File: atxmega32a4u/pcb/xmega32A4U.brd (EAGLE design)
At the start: 51.8 x 18.8 mm, 15 parts

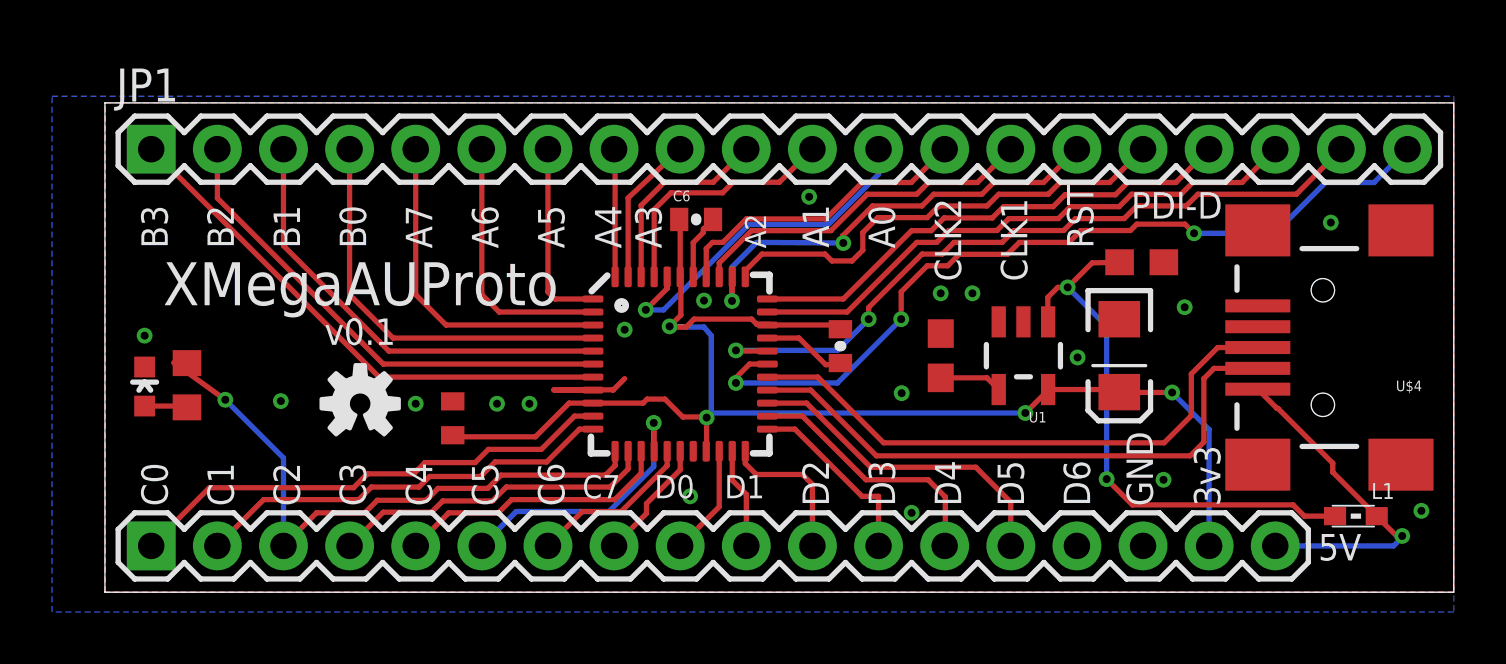
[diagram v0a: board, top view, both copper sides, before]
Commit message: Fix ciruit errors in LDO, added ESD protection to USB circuit - this will be v0.3
v0.3 ready
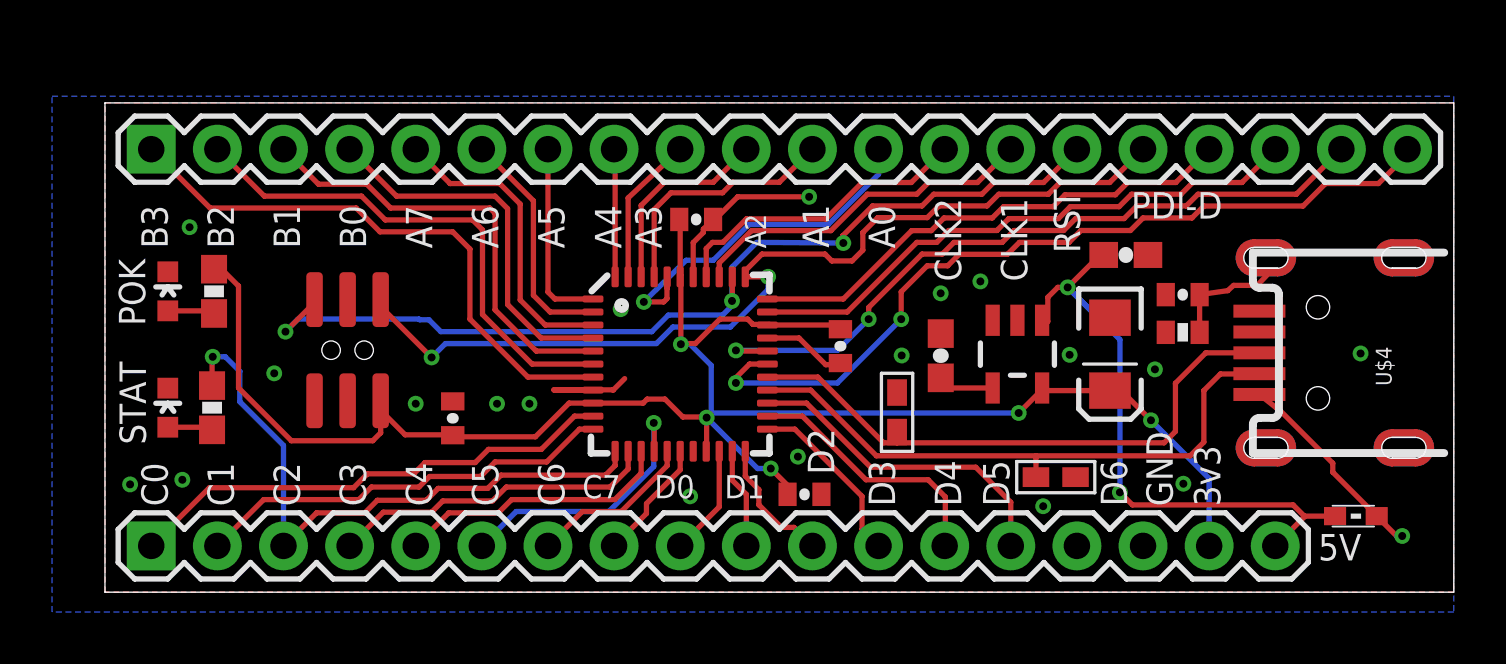
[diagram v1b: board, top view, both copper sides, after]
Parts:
- removed LED2: Blue, SparkFun-LED:LED-0603
- added C4, C7: 0.1uF, SparkFun-Capacitors:0402-CAP
- added ESD1, ESD2: CG0603MLC-05E, JCM:0603-CHIPGUARD
- added POK: Green, SparkFun-LED:LED-0603
- added R2: 1M, SparkFun-Resistors:0402-RES
- added R3: 1k, SparkFun-Passives:0603-RES
- added STATUS: Blue, SparkFun-LED:LED-0603
- added U$7: AVR_PDI_PROG, JCM:AVR_50MIL_PROG
- C1, C3: device rcl:C0603 -> SparkFun-Capacitors:0603-CAP
- C2: device SparkFun-Passives:EIA3216 -> SparkFun-Capacitors:EIA3216
- C5, C6: value (none) -> 0.1uF; device SparkFun-Passives:0402-CAP -> SparkFun-Capacitors:0402-CAP
- C8: value 0.1uF -> 4.7nF; device rcl:C0402 -> SparkFun-Capacitors:0402-CAP
- R1: value 330 -> 1k; device adafruit:R0603 -> SparkFun-Passives:0603-RES
- U$4: value USB-MINIB-5PIN -> USB-MINIB; device SparkFun-Connectors:USB-MINIB -> JCM-Connectors:USB-MINI-B-UX60-MB-5S8
- moved C8 28.4 mm to (42.2, 12.2), turned to 0 degrees
- moved U$6 6.95 mm to (16.4, 11.8), flipped to the bottom
- moved U$4 2.45 mm to (45.1, 9.96), turned to 90 degrees
- moved R1 1.30 mm to (4.88, 7.85)
- moved C1 0.67 mm to (40.0, 13.7)
- moved C2 0.36 mm to (39.4, 9.91)
- moved U1 0.24 mm to (35.8, 9.91)
- renumbered U$1 to UC, U$5 to JP2
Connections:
- new net N$1: POK.A, R3.2
- new net SHLD: C8.2, R2.2, U$4.SHLD1, U$4.SHLD2, U$4.SHLD3, U$4.SHLD4
- net 3.3V: now also C4.1, C7.1, R3.1, U$7.2; no longer C8.1
- net 5V: no longer JP2.18
- net 5VINT: now also JP2.18, U1.3
- net GND: now also C4.2, C7.2, C8.1, ESD1.P$1, ESD2.P$1, POK.C, R2.1, STATUS.C, U$7.6; no longer C8.2, LED2.C
- net N$2: now also STATUS.A; no longer LED2.A
- net PD6/D-: now also ESD1.P$2
- net PD7/D+: now also ESD2.P$2
- net PDI-DATA: now also U$7.1
- net RST: now also U$7.5
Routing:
- net RST: track 17.6 -> 37.4 mm, vias 2 -> 3
- net PDI-DATA: track 17.8 -> 36.2 mm, vias 0 -> 2
- net 3.3V: track 53.7 -> 72.0 mm, vias 4 -> 5
- net 5V: track 13.1 -> 7.96 mm
- net SHLD: track 0.00 -> 4.45 mm
- net GND: track 10.2 -> 14.2 mm, vias 17 -> 19
- net 5VINT: track 21.6 -> 25.1 mm
- net N$1: track 0.00 -> 1.82 mm
- net PB3: track 20.6 -> 22.2 mm
- net PA6: track 10.1 -> 8.99 mm
- net PB0: track 15.6 -> 14.5 mm
- net PA7: track 12.9 -> 11.8 mm
- net PB2: track 19.0 -> 19.8 mm
- net PD2: track 5.75 -> 4.99 mm
- net PD7/D+: track 22.3 -> 22.9 mm
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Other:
- board text added: "J Moreland Engineering LLC 5 May 2013"
- board text added: "POK"
- board text added: "STAT"
- board text added: "v0.3"
- board text removed: "J Moreland Engineering LLC 22 Apr 2013"
- board text removed: "v0.1"
